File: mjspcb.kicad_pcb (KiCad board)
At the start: 2 copper layers, 97.2 x 55.9 mm, 83 parts, among them P1 Batteries, P10 Lipo, P11 grove i2c, P12 grove analog, P13 grove analog, P14 HPMA115S0-XXX, P15 piggyback, P2 serial breakout, P3 I2C breakout, P4 GPS, P5 piezo, P6 BPW34, P7 electrodes, P8 perfboard breakout, P9 reset, Q1 STU60N3LH5, Q2 STU60N3LH5, U1 ATMEGA328P, U2 RFM95W, U3 MCP1700-3302

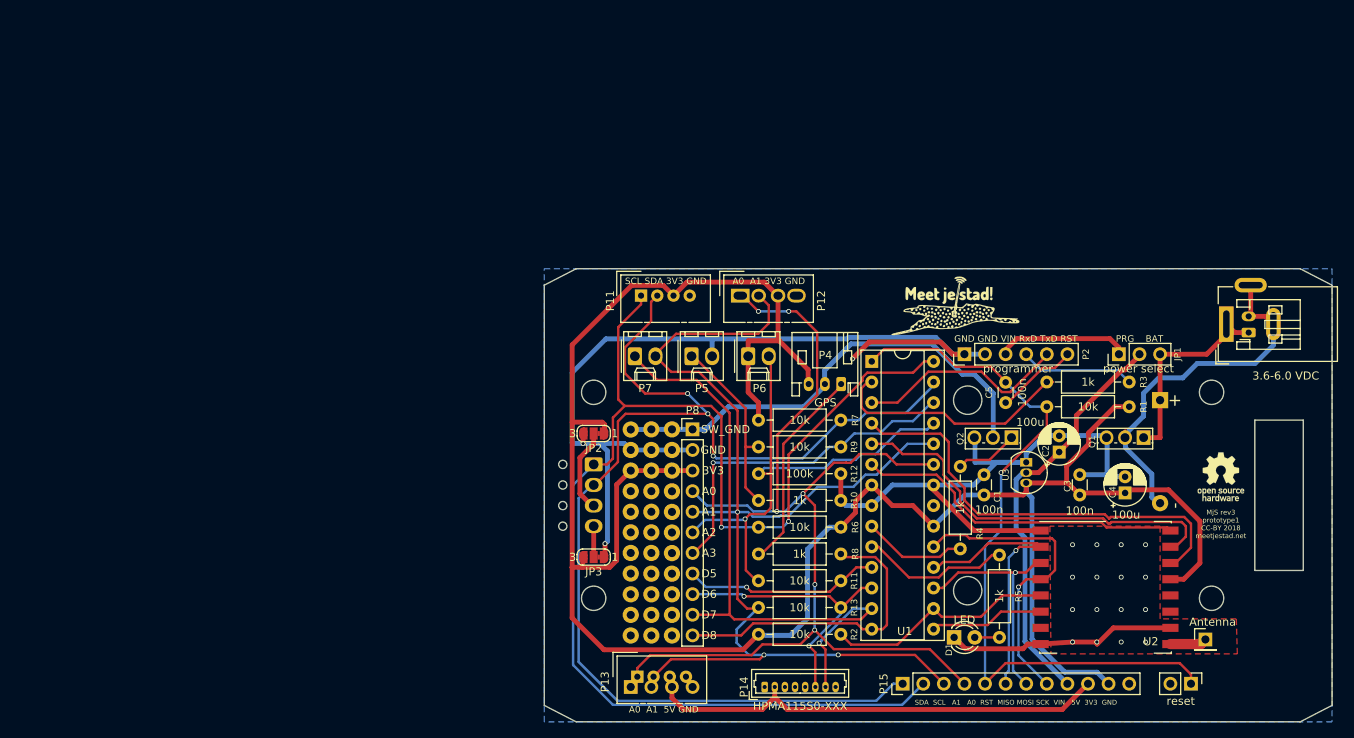
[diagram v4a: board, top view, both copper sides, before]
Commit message: Replace with MJS2020-PROTO2 redesign
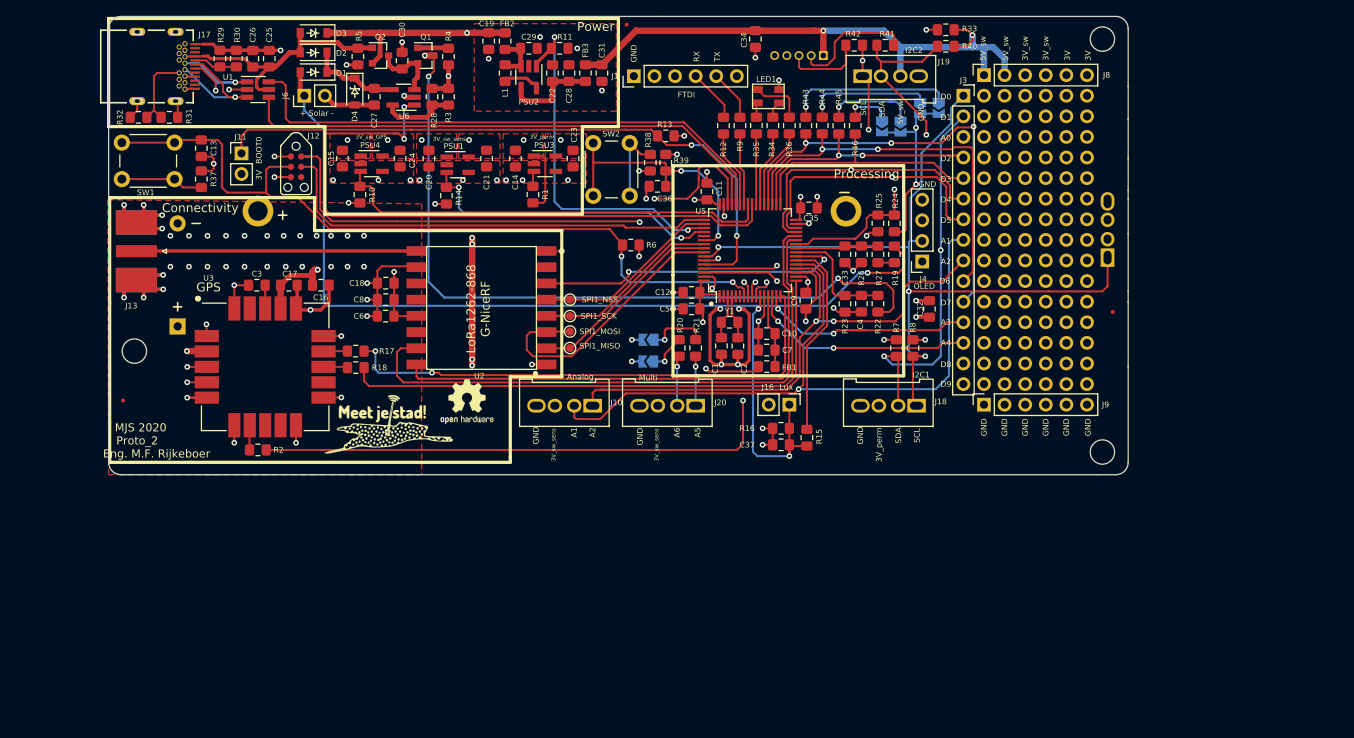
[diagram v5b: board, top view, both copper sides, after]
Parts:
- removed ? (x33): , meetjestad:perf
- removed AE1: Antenna, Connector_PinHeader_2.54mm:PinHeader_1x01_P2.54mm_Vertical
- removed DC1: 2.7 - 6.0 VDC, Connector_BarrelJack:BarrelJack_Wuerth_6941xx301002
- removed H4: MountingHole, MountingHole:MountingHole_3mm
- removed JP1: power select, Connector_PinHeader_2.54mm:PinHeader_1x03_P2.54mm_Vertical
- removed JP2: V1, meetjestad:SolderJumper-3_P1.3mm_Bridged12_RoundedPad1.0x1.5mm_NumberLabels
- removed JP3: V2, meetjestad:SolderJumper-3_P1.3mm_Bridged12_RoundedPad1.0x1.5mm_NumberLabels
- removed LOGO1: Open source hardware, Symbol:OSHW-Logo_5.7x6mm_SilkScreen
- removed LOGO2: MJS Logo, meetjestad:mjs
- removed P1: Batteries, Battery:BatteryHolder_Keystone_2479_3xAAA
- removed P10: Lipo, Connector_JST:JST_PH_S2B-PH-K_1x02_P2.00mm_Horizontal
- removed P11: grove i2c, Connector:NS-Tech_Grove_1x04_P2mm_Vertical
- removed P12: grove analog, meetjestad:NS-Tech_Grove_1x04_P2mm_P2.54mm_Vertical
- removed P13: grove analog, meetjestad:NS-Tech_Grove_1x04_P2mm_P2.54mm_Vertical_Alternative
- removed P14: HPMA115S0-XXX, Connector_Molex:Molex_PicoBlade_53047-0810_1x08_P1.25mm_Vertical
- removed P15: piggyback, Connector_PinHeader_2.54mm:PinHeader_1x12_P2.54mm_Vertical
- removed P2: serial breakout, Connector_PinHeader_2.54mm:PinHeader_1x06_P2.54mm_Vertical
- removed P3: I2C breakout, meetjestad:Molex_KK-254_44812-0004_1x04_P2.54mm_Vertical
- removed P4: GPS, Connector_JST:JST_PH_S3B-PH-K_1x03_P2.00mm_Horizontal
- removed P5: piezo, Connector_Molex:Molex_KK-254_AE-6410-02A_1x02_P2.54mm_Vertical
- removed P6: BPW34, Connector_Molex:Molex_KK-254_AE-6410-02A_1x02_P2.54mm_Vertical
- removed P7: electrodes, Connector_Molex:Molex_KK-254_AE-6410-02A_1x02_P2.54mm_Vertical
- removed P8: perfboard breakout, Connector_PinHeader_2.54mm:PinHeader_1x11_P2.54mm_Vertical
- removed P9: reset, Connector_PinHeader_2.54mm:PinHeader_1x02_P2.54mm_Vertical
- added C10: 100nF, Capacitor_SMD:C_0805_2012Metric_Pad1.15x1.40mm_HandSolder, F.Cu at (161.0, 100.7)
- added C11: 100nF, Capacitor_SMD:C_0805_2012Metric_Pad1.15x1.40mm_HandSolder, F.Cu at (153.7, 83.2)
- added C12: 100nF, Capacitor_SMD:C_0805_2012Metric_Pad1.15x1.40mm_HandSolder, F.Cu at (151.8, 95.6)
- added C13: 100nF, Capacitor_SMD:C_0805_2012Metric_Pad1.15x1.40mm_HandSolder, F.Cu at (91.3, 77.9)
- added C14: 1uF, Capacitor_SMD:C_0805_2012Metric_Pad1.15x1.40mm_HandSolder, F.Cu at (130.0, 79.1)
- added C15: 1uF, Capacitor_SMD:C_0805_2012Metric_Pad1.15x1.40mm_HandSolder, F.Cu at (108.7, 79.1)
- added C16: 4.7uF, Capacitor_SMD:C_0805_2012Metric_Pad1.15x1.40mm_HandSolder, F.Cu at (106.0, 94.7)
- added C17: 100nF, Capacitor_SMD:C_0805_2012Metric_Pad1.15x1.40mm_HandSolder, F.Cu at (102.1, 94.7)
- added C18: 4.7uF, Capacitor_SMD:C_0805_2012Metric_Pad1.15x1.40mm_HandSolder, F.Cu at (114.1, 94.5)
- added C19: 1uF, Capacitor_SMD:C_0805_2012Metric_Pad1.15x1.40mm_HandSolder, F.Cu at (126.7, 64.6)
- added C20: 1uF, Capacitor_SMD:C_0805_2012Metric_Pad1.15x1.40mm_HandSolder, F.Cu at (119.4, 79.1)
- added C21: 1uF, Capacitor_SMD:C_0805_2012Metric_Pad1.15x1.40mm_HandSolder, F.Cu at (126.5, 79.1)
- added C22: 4.7uF, Capacitor_SMD:C_0805_2012Metric_Pad1.15x1.40mm_HandSolder, F.Cu at (134.6, 68.6)
- added C23: 1uF, Capacitor_SMD:C_0805_2012Metric_Pad1.15x1.40mm_HandSolder, F.Cu at (137.2, 79.1)
- added C24: 1uF, Capacitor_SMD:C_0805_2012Metric_Pad1.15x1.40mm_HandSolder, F.Cu at (115.8, 79.1)
- added C25: 100nF, Capacitor_SMD:C_0805_2012Metric_Pad1.15x1.40mm_HandSolder, F.Cu at (99.7, 66.8)
- added C26: 1uF, Capacitor_SMD:C_0805_2012Metric_Pad1.15x1.40mm_HandSolder, F.Cu at (97.7, 66.8)
- added C27: 4.7uF, Capacitor_SMD:C_0805_2012Metric_Pad1.15x1.40mm_HandSolder, F.Cu at (112.6, 71.5)
- added C28: 4.7uF, Capacitor_SMD:C_0805_2012Metric_Pad1.15x1.40mm_HandSolder, F.Cu at (136.7, 68.6)
- added C29: 4.7uF, Capacitor_SMD:C_0805_2012Metric_Pad1.15x1.40mm_HandSolder, F.Cu at (131.7, 65.5)
- added C30: 4.7uF, Capacitor_SMD:C_0805_2012Metric_Pad1.15x1.40mm_HandSolder, F.Cu at (116.1, 67.0)
- added C31: 1uF, Capacitor_SMD:C_0805_2012Metric_Pad1.15x1.40mm_HandSolder, F.Cu at (140.7, 68.6)
- added C32: 100nF, Capacitor_SMD:C_0805_2012Metric_Pad1.15x1.40mm_HandSolder, F.Cu at (181.1, 97.7)
- added C33: 100nF, Capacitor_SMD:C_0805_2012Metric_Pad1.15x1.40mm_HandSolder, F.Cu at (170.7, 90.9)
- added C34: 100nF, Capacitor_SMD:C_0805_2012Metric_Pad1.15x1.40mm_HandSolder, F.Cu at (159.6, 64.4)
- added C35: 100nF, Capacitor_SMD:C_0805_2012Metric_Pad1.15x1.40mm_HandSolder, F.Cu at (166.2, 85.2)
- added C36: 100nF, Capacitor_SMD:C_0805_2012Metric_Pad1.15x1.40mm_HandSolder, F.Cu at (147.6, 82.5)
- added C37: 100nF, Capacitor_SMD:C_0805_2012Metric_Pad1.15x1.40mm_HandSolder, F.Cu at (162.8, 114.4)
- added C6: 100nF, Capacitor_SMD:C_0805_2012Metric_Pad1.15x1.40mm_HandSolder, F.Cu at (114.0, 98.6)
- added C7: 1uF, Capacitor_SMD:C_0805_2012Metric_Pad1.15x1.40mm_HandSolder, F.Cu at (161.0, 102.7)
- added C8: 4.7uF, Capacitor_SMD:C_0805_2012Metric_Pad1.15x1.40mm_HandSolder, F.Cu at (114.1, 96.5)
- added C9: 100nF, Capacitor_SMD:C_0805_2012Metric_Pad1.15x1.40mm_HandSolder, F.Cu at (165.9, 96.6)
- added D2: MBR120VLSFT3G, meetjestad:Diode_SMD-SOD_123, F.Cu at (105.4, 63.3)
- added D3: MBR120VLSFT3G, meetjestad:Diode_SMD-SOD_123, F.Cu at (105.4, 60.9)
- added D4: 6,2V, meetjestad:D_SOD-123, F.Cu at (112.9, 71.0)
- added FB1: Ferrite_Bead, Resistor_SMD:R_0805_2012Metric_Pad1.15x1.40mm_HandSolder, F.Cu at (161.0, 104.8)
- added FB2: Ferrite_Bead, Resistor_SMD:R_0805_2012Metric_Pad1.15x1.40mm_HandSolder, F.Cu at (128.8, 64.6)
- added FB3: Ferrite_Bead, Resistor_SMD:R_0805_2012Metric_Pad1.15x1.40mm_HandSolder, F.Cu at (138.7, 68.6)
- added FID1: Fiducial, Fiducial:Fiducial_0.5mm_Mask1mm, F.Cu at (81.7, 109.0)
- added FID2: Fiducial, Fiducial:Fiducial_0.5mm_Mask1mm, F.Cu at (143.8, 62.6)
- added FID3: Fiducial, Fiducial:Fiducial_0.5mm_Mask1mm, F.Cu at (203.7, 98.0)
- added J1: FTDI, Connector_PinHeader_2.54mm:PinHeader_1x06_P2.54mm_Vertical, F.Cu at (144.7, 69.0)
- added J10: Analog, meetjestad:Grove_4pin&Header_4pin, F.Cu at (135.7, 108.3)
- added J11: BOOT0, Connector_PinHeader_2.54mm:PinHeader_1x02_P2.54mm_Vertical, F.Cu at (96.3, 78.5)
- added J12: Tag connect, meetjestad:Tag connect, F.Cu at (102.4, 78.9)
- added J13: Conn_Coaxial, meetjestad:SMA connector edge mount, F.Cu at (79.0, 97.8)
- added J14: Lithium Ion, meetjestad:BatteryHolder_18650-PC2, B.Cu at (134.6, 85.6)
- added J15: Temp/Hum, meetjestad:Grove_4pin&Header_4pin, B.Cu at (201.8, 87.5)
- added J16: BPW34, Connector_PinHeader_2.54mm:PinHeader_1x02_P2.54mm_Vertical, F.Cu at (163.8, 109.5)
- added J17: USB_C_connector, 632723300011_Eagle_WR-USB_rev20b:632723100011, F.Cu at (84.6, 67.8)
- added J18: I2C 3V_perm, meetjestad:Grove_4pin&Header_4pin, F.Cu at (175.7, 108.3)
- added J19: I2C 5V_SW, meetjestad:Grove_4pin&Header_4pin, F.Cu at (176.7, 70.2)
- added J20: Multi, meetjestad:Grove_4pin&Header_4pin, F.Cu at (148.4, 108.3)
- added J3: Prototype header, Connector_PinSocket_2.54mm:PinSocket_1x15_P2.54mm_Vertical, F.Cu at (185.3, 71.4)
- added J4: Oled, Connector_PinSocket_2.54mm:PinSocket_1x04_P2.54mm_Vertical, F.Cu at (180.2, 91.8)
- added J5: Conn_01x02_Male, meetjestad:Battery__holder, B.Cu at (110.0, 110.0)
- added J6: Solar, Connector_PinHeader_2.54mm:PinHeader_1x02_P2.54mm_Vertical, F.Cu at (104.0, 71.4)
- added J7: Particulate matter, meetjestad:B5B-ZR, B.Cu at (165.5, 63.9)
- added J8: Prototype power, Connector_PinSocket_2.54mm:PinSocket_1x06_P2.54mm_Vertical, F.Cu at (187.8, 68.8)
- added J9: Prototype GND, Connector_PinSocket_2.54mm:PinSocket_1x06_P2.54mm_Vertical, F.Cu at (187.8, 109.5)
- added L1: 4.7uH, Resistor_SMD:R_0805_2012Metric_Pad1.15x1.40mm_HandSolder, F.Cu at (128.8, 68.6)
- added LED1: JT-S3030_RGB_LED, meetjestad:JT-S3030_RGB_LED, F.Cu at (160.0, 70.6)
- added Logo_kitt1: Logo_Open_Hardware_Small, meetjestad:Kitt_logo, B.Cu at (86.4, 109.6)
- added Logo_mjs1: Logo_Open_Hardware_Small, meetjestad:mjs_logo, F.Cu at (113.7, 107.4)
- added Logo_mjs2: Logo_Open_Hardware_Small, Symbol:OSHW-Logo2_7.3x6mm_SilkScreen, F.Cu at (124.1, 109.1)
- added PSU1: TPS7A02, Package_TO_SOT_SMD:SOT-23-5_HandSoldering, F.Cu at (122.9, 79.9)
- added PSU2: XC9140A501MR-G, Package_TO_SOT_SMD:SOT-23-5_HandSoldering, F.Cu at (131.7, 69.1)
- added PSU3: TPS7A02, Package_TO_SOT_SMD:SOT-23-5_HandSoldering, F.Cu at (133.7, 79.8)
- added PSU4: TPS7A02, Package_TO_SOT_SMD:SOT-23-5_HandSoldering, F.Cu at (112.3, 79.8)
- added R14: 100k, Resistor_SMD:R_0805_2012Metric_Pad1.15x1.40mm_HandSolder, F.Cu at (121.5, 83.7)
- added R15: 10k, Resistor_SMD:R_0805_2012Metric_Pad1.15x1.40mm_HandSolder, F.Cu at (166.0, 113.5)
- added R16: 100k, Resistor_SMD:R_0805_2012Metric_Pad1.15x1.40mm_HandSolder, F.Cu at (162.8, 112.4)
- added R17: 1k, Resistor_SMD:R_0805_2012Metric_Pad1.15x1.40mm_HandSolder, F.Cu at (110.4, 102.9)
- added R18: 1k, Resistor_SMD:R_0805_2012Metric_Pad1.15x1.40mm_HandSolder, F.Cu at (110.4, 104.9)
- added R19: 1M, Resistor_SMD:R_0805_2012Metric_Pad1.15x1.40mm_HandSolder, F.Cu at (176.8, 90.9)
- added R20: 10k, Resistor_SMD:R_0805_2012Metric_Pad1.15x1.40mm_HandSolder, F.Cu at (150.2, 102.5)
- added R21: 10k, Resistor_SMD:R_0805_2012Metric_Pad1.15x1.40mm_HandSolder, F.Cu at (152.3, 102.5)
- added R22: 1M, Resistor_SMD:R_0805_2012Metric_Pad1.15x1.40mm_HandSolder, F.Cu at (174.8, 97.0)
- added R23: 1M, Resistor_SMD:R_0805_2012Metric_Pad1.15x1.40mm_HandSolder, F.Cu at (170.7, 97.0)
- added R24: 1M, Resistor_SMD:R_0805_2012Metric_Pad1.15x1.40mm_HandSolder, F.Cu at (176.8, 87.1)
- added R25: 100k, Resistor_SMD:R_0805_2012Metric_Pad1.15x1.40mm_HandSolder, F.Cu at (174.8, 87.1)
- added R26: 1M, Resistor_SMD:R_0805_2012Metric_Pad1.15x1.40mm_HandSolder, F.Cu at (174.8, 90.9)
- added R27: 1M, Resistor_SMD:R_0805_2012Metric_Pad1.15x1.40mm_HandSolder, F.Cu at (172.7, 90.9)
- added R28: 10k, Resistor_SMD:R_0805_2012Metric_Pad1.15x1.40mm_HandSolder, F.Cu at (119.8, 71.5)
- added R29: 10k, Resistor_SMD:R_0805_2012Metric_Pad1.15x1.40mm_HandSolder, F.Cu at (93.6, 66.8)
- added R30: 10k, Resistor_SMD:R_0805_2012Metric_Pad1.15x1.40mm_HandSolder, F.Cu at (95.6, 66.8)
- added R31: 10k, Resistor_SMD:R_0805_2012Metric_Pad1.15x1.40mm_HandSolder, F.Cu at (87.4, 74.0)
- added R32: 10k, Resistor_SMD:R_0805_2012Metric_Pad1.15x1.40mm_HandSolder, F.Cu at (83.6, 74.0)
- added R33: 10k, Resistor_SMD:R_0805_2012Metric_Pad1.15x1.40mm_HandSolder, F.Cu at (183.1, 63.2)
- added R34: 1k, Resistor_SMD:R_0805_2012Metric_Pad1.15x1.40mm_HandSolder, F.Cu at (161.8, 75.0)
- added R35: 1k, Resistor_SMD:R_0805_2012Metric_Pad1.15x1.40mm_HandSolder, F.Cu at (159.8, 75.0)
- added R36: 1k, Resistor_SMD:R_0805_2012Metric_Pad1.15x1.40mm_HandSolder, F.Cu at (163.8, 75.0)
- added R37: 100, Resistor_SMD:R_0805_2012Metric_Pad1.15x1.40mm_HandSolder, F.Cu at (91.3, 81.7)
- added R38: 100, Resistor_SMD:R_0805_2012Metric_Pad1.15x1.40mm_HandSolder, F.Cu at (146.7, 79.6)
- added R39: 10k, Resistor_SMD:R_0805_2012Metric_Pad1.15x1.40mm_HandSolder, F.Cu at (148.6, 79.6)
- added R40: 10k, Resistor_SMD:R_0805_2012Metric_Pad1.15x1.40mm_HandSolder, F.Cu at (183.1, 65.3)
- added R41: 1k, Resistor_SMD:R_0805_2012Metric_Pad1.15x1.40mm_HandSolder, F.Cu at (175.7, 65.2)
- added R42: 1k, Resistor_SMD:R_0805_2012Metric_Pad1.15x1.40mm_HandSolder, F.Cu at (171.8, 65.2)
- added R43: 10k, Resistor_SMD:R_0805_2012Metric_Pad1.15x1.40mm_HandSolder, F.Cu at (165.9, 75.0)
- added R44: 10k, Resistor_SMD:R_0805_2012Metric_Pad1.15x1.40mm_HandSolder, F.Cu at (167.9, 75.0)
- added R45: 10k, Resistor_SMD:R_0805_2012Metric_Pad1.15x1.40mm_HandSolder, F.Cu at (169.9, 75.1)
- added R46: 10k, Resistor_SMD:R_0805_2012Metric_Pad1.15x1.40mm_HandSolder, F.Cu at (172.0, 75.1)
- added SP1: SolderJumper_2_Open, Jumper:SolderJumper-2_P1.3mm_Open_TrianglePad1.0x1.5mm, B.Cu at (146.4, 104.1)
- added SP2: SolderJumper_2_Open, Jumper:SolderJumper-2_P1.3mm_Open_TrianglePad1.0x1.5mm, B.Cu at (146.5, 101.5)
- added SP3: SolderJumper_2_Open, Jumper:SolderJumper-2_P1.3mm_Open_TrianglePad1.0x1.5mm, B.Cu at (182.2, 72.9)
- added SP4: SolderJumper_2_Open, Jumper:SolderJumper-2_P1.3mm_Open_TrianglePad1.0x1.5mm, B.Cu at (180.0, 72.9)
- added SP5: SolderJumper_2_Open, Jumper:SolderJumper-2_P1.3mm_Open_TrianglePad1.0x1.5mm, B.Cu at (177.5, 75.2)
- added SP6: SolderJumper_2_Open, Jumper:SolderJumper-2_P1.3mm_Open_TrianglePad1.0x1.5mm, B.Cu at (175.3, 75.1)
- added SW1: SW_Push, Button_Switch_THT:SW_PUSH_6mm, F.Cu at (88.0, 81.7)
- added SW2: SW_Push, Button_Switch_THT:SW_PUSH_6mm, F.Cu at (144.1, 77.2)
- added TP1: TestPoint_Small, TestPoint:TestPoint_Pad_D1.0mm, F.Cu at (136.8, 96.5)
- added TP2: TestPoint_Small, TestPoint:TestPoint_Pad_D1.0mm, F.Cu at (136.8, 98.6)
- added TP3: TestPoint_Small, TestPoint:TestPoint_Pad_D1.0mm, F.Cu at (136.8, 100.5)
- added TP4: TestPoint_Small, TestPoint:TestPoint_Pad_D1.0mm, F.Cu at (136.8, 102.5)
- added TP5: Sticker field, meetjestad:Sticker field, B.Cu at (110.0, 117.3)
- added TP6: Flash OK, meetjestad:Flash OK, B.Cu at (132.8, 113.7)
- added TP7: Test OK, meetjestad:Test OK, B.Cu at (159.3, 115.7)
- added U4: PrototypeGrid, meetjestad:Prototype grid, F.Cu at (187.8, 71.4)
- added U5: STM32L072RBTx-meetjestad, meetjestad:STM32F072_LQFP-64, F.Cu at (151.0, 90.4)
- added U6: MCP73831, Package_TO_SOT_SMD:SOT-23-5_HandSoldering, F.Cu at (116.3, 71.6)
- added Y1: 32kHz, Resistor_SMD:R_0805_2012Metric_Pad1.15x1.40mm_HandSolder, F.Cu at (156.5, 99.3)
- C1: value 100n -> 12.5pF; footprint Capacitor_THT:C_Disc_D3.0mm_W1.6mm_P2.50mm -> Capacitor_SMD:C_0805_2012Metric_Pad1.15x1.40mm_HandSolder
- C2: value 100u -> 12.5pF; footprint Capacitor_THT:CP_Radial_D5.0mm_P2.00mm -> Capacitor_SMD:C_0805_2012Metric_Pad1.15x1.40mm_HandSolder
- C3, C5: value 100n -> 100nF; footprint Capacitor_THT:C_Disc_D3.0mm_W1.6mm_P2.50mm -> Capacitor_SMD:C_0805_2012Metric_Pad1.15x1.40mm_HandSolder
- C4: value 100u -> 100nF; footprint Capacitor_THT:CP_Radial_D5.0mm_P2.00mm -> Capacitor_SMD:C_0805_2012Metric_Pad1.15x1.40mm_HandSolder
- D1: value LED -> MBR120VLSFT3G; footprint LED_THT:LED_D3.0mm -> meetjestad:Diode_SMD-SOD_123
- H1, H2, H3: footprint MountingHole:MountingHole_3mm -> meetjestad:Mounting_hole
- Q1, Q2: value STU60N3LH5 -> DMP2035U-7; footprint Package_TO_SOT_THT:TO-251-3_Vertical -> Package_TO_SOT_SMD:SOT-23
- R1, R2, R9: value 10k -> 1k; footprint Resistor_THT:R_Axial_DIN0207_L6.3mm_D2.5mm_P10.16mm_Horizontal -> Resistor_SMD:R_0805_2012Metric_Pad1.15x1.40mm_HandSolder
- R10: value 1k -> 100k; footprint Resistor_THT:R_Axial_DIN0207_L6.3mm_D2.5mm_P10.16mm_Horizontal -> Resistor_SMD:R_0805_2012Metric_Pad1.15x1.40mm_HandSolder
- R11: value 10k -> 100k; footprint Resistor_THT:R_Axial_DIN0207_L6.3mm_D2.5mm_P10.16mm_Horizontal -> Resistor_SMD:R_0805_2012Metric_Pad1.15x1.40mm_HandSolder
- R12: value 100k -> 1k; footprint Resistor_THT:R_Axial_DIN0207_L6.3mm_D2.5mm_P10.16mm_Horizontal -> Resistor_SMD:R_0805_2012Metric_Pad1.15x1.40mm_HandSolder
- R13, R6, R7: footprint Resistor_THT:R_Axial_DIN0207_L6.3mm_D2.5mm_P10.16mm_Horizontal -> Resistor_SMD:R_0805_2012Metric_Pad1.15x1.40mm_HandSolder
- R3, R4, R5, R8: value 1k -> 10k; footprint Resistor_THT:R_Axial_DIN0207_L6.3mm_D2.5mm_P10.16mm_Horizontal -> Resistor_SMD:R_0805_2012Metric_Pad1.15x1.40mm_HandSolder
- U1: value ATMEGA328P -> USBLC-2SC6; footprint Package_DIP:DIP-28_W7.62mm_Socket -> Package_TO_SOT_SMD:SOT-23-6_Handsoldering
- U2: value RFM95W -> LoRa_1262_G-NiceRF; footprint RF_Module:HOPERF_RFM9XW_SMD -> meetjestad:LoRa_1262_G-NiceRF
- U3: value MCP1700-3302 -> GPS; footprint Package_TO_SOT_THT:TO-92_Inline -> meetjestad:GPS_ublox-SAM-M8Q
- moved D1 107.0 mm to (105.4, 65.7)
- moved C3 104.7 mm to (98.2, 94.7), turned to 0 degrees
- moved Q1 100.3 mm to (119.0, 66.4), turned to 0 degrees
- moved R5 100.2 mm to (110.6, 66.5)
- moved U3 96.2 mm to (99.4, 94.6), turned to 0 degrees
- moved R3 91.0 mm to (121.8, 71.5), turned to 90 degrees
- moved Q2 91.0 mm to (113.4, 66.4), turned to 0 degrees
- moved U1 82.8 mm to (98.3, 70.6)
- moved R4 80.9 mm to (121.8, 66.5)
- moved R1 78.0 mm to (132.2, 83.6), turned to 270 degrees
- moved H1 76.4 mm to (202.4, 64.4)
- moved U2 74.2 mm to (133.9, 104.5), turned to 180 degrees
- moved R11 70.1 mm to (135.5, 65.5)
- moved R2 65.8 mm to (98.3, 115.1), turned to 180 degrees
- moved H2 64.3 mm to (83.1, 102.9)
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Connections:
- C1 pad 1: VCC -> Net-(C1-Pad1)
- C2 pad 1: VIN -> Net-(C2-Pad1)
- C3 pad 1: VCC -> GND
- C3 pad 2: GND -> Net-(C3-Pad2)
- C4 pad 1: VCC -> PC4
- C5 pad 1: Net-(C5-Pad1) -> 3V-perm_CPU
- C5 pad 2: RST -> GND
- D1 pad 1: GND -> Solar
- D1 pad 2: Net-(D1-Pad2) -> Net-(C27-Pad2)
- Q1 pad 1: +BATT -> Net-(Q1-Pad1)
- Q1 pad 2: -BATT -> Net-(C30-Pad1)
- Q1 pad 3: GND -> +BATT
- Q2 pad 1: Net-(Q2-Pad1) -> VBUS
- Q2 pad 2: SW_GND -> Vin
- Q2 pad 3: GND -> Net-(C30-Pad1)
- R1 pad 1: VCC -> Net-(PSU3-Pad3)
- R1 pad 2: RST -> Vin
- R10 pad 1: Net-(P5-Pad1) -> PA8
- R11 pad 1: A2 -> PC10
- R11 pad 2: D5 -> GND
- R12 pad 1: A2 -> Net-(J1-Pad4)
- R12 pad 2: GND -> PA10
- R13 pad 1: A1 -> BOOT0
- R13 pad 2: D6 -> GND
- R2 pad 1: VCC -> PC2
- R2 pad 2: D10 -> Net-(R2-Pad2)
- R3 pad 2: RXD -> GND
- R4 pad 1: Net-(Q2-Pad1) -> Net-(Q1-Pad1)
- R4 pad 2: X1 -> GND
- R5 pad 1: X2 -> VBUS
- R5 pad 2: Net-(D1-Pad2) -> GND
- R6 pad 1: VCC -> 3V-perm_CPU
- R6 pad 2: SCL -> NRST
- R7 pad 1: VCC -> PB7
- R7 pad 2: SDA -> 3V-perm_CPU
- R8 pad 1: Net-(P4-Pad1) -> PB6
- R8 pad 2: D8 -> 3V-perm_CPU
- R9 pad 1: Net-(P5-Pad1) -> Net-(J1-Pad5)
- R9 pad 2: A3 -> PA9
- U1 pad 1: RST -> Net-(J17-PadA7)
- U1 pad 2: RXD -> GND
- U1 pad 3: TXD -> Net-(J17-PadA6)
- U1 pad 4: D2 -> PA12
- U1 pad 5: D3 -> VBUS
- U1 pad 6: D4 -> PA11
- U2 pad 13: VCC -> 3V-perm_CPU
- U2 pad 14: D2 -> Net-(U2-Pad14)
- U2 pad 15: D3 -> PB1
- U2 pad 16: D4 -> PB2
- U2 pad 2: MISO -> PB4
- U2 pad 3: MOSI -> PB5
- U2 pad 4: SCK -> PB3
- U2 pad 5: D10 -> PA15
- U2 pad 6: D9 -> PA7
- U3 pad 2: VIN -> 3V-sw_GPS
- U3 pad 3: VCC -> 3V-perm_CPU
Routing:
- net VCC: track 280.6 -> 0.00 mm
- net 3V-sw_sens: track 0.00 -> 199.2 mm, vias 0 -> 9
- net SCL: track 164.4 -> 0.00 mm, vias 2 -> 0
- net SDA: track 146.8 -> 0.00 mm, vias 3 -> 0
- net +BATT: track 26.0 -> 168.7 mm, vias 0 -> 3
- net A1: track 141.9 -> 0.00 mm, vias 3 -> 0
- net A0: track 134.9 -> 0.00 mm, vias 6 -> 0
- net Solar: track 0.00 -> 106.8 mm, vias 0 -> 1
- net PB6: track 0.00 -> 100.0 mm, vias 0 -> 3
- net PB7: track 0.00 -> 98.4 mm, vias 0 -> 3
- net NRST: track 0.00 -> 97.5 mm, vias 0 -> 2
- net RST: track 91.2 -> 0.00 mm, vias 1 -> 0
- net 3V-perm_CPU: track 0.00 -> 88.3 mm, vias 0 -> 15
- net PA5: track 0.00 -> 87.6 mm, vias 0 -> 1
- net PC2: track 0.00 -> 83.8 mm, vias 0 -> 2
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- added copper zone on F.Cu, net 3V-perm_CPU
- added copper zone on In2.Cu, net 3V-perm_CPU
- added copper zone on F.Cu, net 3V-sw_GPS
- added copper zone on F.Cu, net 3V-sw_sens
- added copper zone on In1.Cu, net GND
- added copper zone on F.Cu, net Vin
- removed copper zone on B.Cu, net GND
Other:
- board size 97.2 x 55.9 mm -> 125.7 x 56.5 mm
- copper layers 2 -> 4
- net class 3v cpu added: clearance 0.2, trace_width 0.35, via_dia 0.7, via_drill 0.35
- net class Antenna added: clearance 0.9, trace_width 0.43, via_dia 0.7, via_drill 0.35
- net class Default: trace_width 0.3 -> 0.25; via_dia 0.6 -> 0.7; via_drill 0.4 -> 0.35
- net class antenna removed
- net class power: clearance 0.2 -> 0.3; via_dia 0.6 -> 0.7; via_drill 0.4 -> 0.35
- rule pad_to_mask_clearance: 0 -> 0.051
- board text added: "+ Solar -"
- board text added: "3V"
- board text added: "3V_perm"
- board text added: "3V_sw"
- board text added: "3V_sw_GPS"
- board text added: "3V_sw_sens"
- board text added: "5V_sw"
- board text added: "A4"
- board text added: "A5"
- board text added: "A6"
- board text added: "Analog"
- board text added: "BOOT0"
- board text added: "Connectivity"
- board text added: "D0"
- board text added: "D1"
- board text added: "D2"
- board text added: "D3"
- board text added: "D4"
- board text added: "D9"
- board text added: "FTDI"
- board text added: "GPS"
- board text added: "I2C1"
- board text added: "I2C2"
- board text added: "I2C2_SCL"
- board text added: "I2C2_SDA"
- board text added: "LoRa1262-868 G-NiceRF"
- board text added: "Lux"
- board text added: "MJS 2020 Proto_2 Eng. M.F. Rijkeboer"
- board text added: "Multi"
- board text added: "OLED"
- board text added: "Particulate matter"
- board text added: "Power"
- board text added: "Processing"
- board text added: "RX"
- board text added: "SCL"
- board text added: "SDA"
- board text added: "SPI1_MISO"
- board text added: "SPI1_MOSI"
- board text added: "SPI1_NSS"
- board text added: "SPI1_SCK"
- board text added: "TX"
- board text added: "Temp/hum"
- board text removed: "+"
- board text removed: "-"
- board text removed: "3.6-6.0 VDC"
- board text removed: "3V3"
- board text removed: "A0 A1 3V3 GND"
- board text removed: "A0 A1 5V GND"
- board text removed: "GND GND VIN RxD TxD RST"
- board text removed: "I2C breakout"
- board text removed: "ID"
- board text removed: "MjS rev3 prototype1 CC-BY 2018 meetjestad.net"
- board text removed: "PRG BAT"
- board text removed: "SCL SDA 3V3 GND"
- board text removed: "SDA SCL A1 A0 RST MISO MOSI SCK VIN 5V 3V3 GND"
- board text removed: "SW_GND"
- board text removed: "power select"
- board text removed: "programmer"

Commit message: Update to MJS2020-PROTO3
See CHANGELOG.md for detailed changes.
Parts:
- removed J11: BOOT0, Connector_PinHeader_2.54mm:PinHeader_1x02_P2.54mm_Vertical
- removed LED1: JT-S3030_RGB_LED, meetjestad:JT-S3030_RGB_LED
- removed the PSU1 at (122.9, 79.9)
- removed SP3, SP4, SP5, SP6: SolderJumper_2_Open, Jumper:SolderJumper-2_P1.3mm_Open_TrianglePad1.0x1.5mm
- removed TP1, TP2, TP3, TP4: TestPoint_Small, TestPoint:TestPoint_Pad_D1.0mm
- added C38: 100nF, Capacitor_SMD:C_0805_2012Metric_Pad1.15x1.40mm_HandSolder, F.Cu at (167.9, 78.9)
- added C39: 100nF, Capacitor_SMD:C_0805_2012Metric_Pad1.15x1.40mm_HandSolder, B.Cu at (216.8, 85.1)
- added C40: 100nF, Capacitor_SMD:C_0805_2012Metric_Pad1.15x1.40mm_HandSolder, B.Cu at (182.9, 91.4)
- added D5: LED, LED_SMD:LED_0805_2012Metric, F.Cu at (114.6, 74.9)
- added D6: LED_RGB, meetjestad:JTS3535, F.Cu at (140.6, 86.0)
- added J2: Conn_01x16_Female, Connector_PinSocket_2.54mm:PinSocket_1x16_P2.54mm_Vertical, F.Cu at (185.4, 109.2)
- added Logo_mjs3: Logo_Open_Hardware_Small, meetjestad:mjs-logo-22mm, F.Cu at (106.7, 106.4)
- added Logo_mjs4: Logo_Open_Hardware_Small, Symbol:OSHW-Logo2_7.3x6mm_SilkScreen, B.Cu at (180.8, 75.9)
- added PSU2: TPS7A02, Package_TO_SOT_SMD:SOT-23-5_HandSoldering, F.Cu at (122.9, 82.2)
- added R47: 1M, Resistor_SMD:R_0805_2012Metric_Pad1.15x1.40mm_HandSolder, F.Cu at (165.9, 78.9)
- added R48: 10k, Resistor_SMD:R_0805_2012Metric_Pad1.15x1.40mm_HandSolder, F.Cu at (122.2, 74.9)
- added R49: 10k, Resistor_SMD:R_0805_2012Metric_Pad1.15x1.40mm_HandSolder, B.Cu at (172.3, 81.8)
- added R50: 10k, Resistor_SMD:R_0805_2012Metric_Pad1.15x1.40mm_HandSolder, B.Cu at (176.2, 80.8)
- added SW3: SW_Push, meetjestad:Switch_Header2.54_Combi, F.Cu at (96.5, 76.2)
- added U7: MCP9808_MSOP, Package_SO:MSOP-8_3x3mm_P0.65mm, B.Cu at (216.5, 90.2)
- added U8: SST26VF032B, Package_SO:SOIJ-8_5.3x5.3mm_P1.27mm, B.Cu at (179.4, 85.3)
- H1, H2, H3: footprint meetjestad:Mounting_hole -> MountingHole:MountingHole_3.2mm_M3
- J10, J18, J19, J20: footprint meetjestad:Grove_4pin&Header_4pin -> meetjestad:2,54_2.0pitchCombi
- J12: value Tag connect -> SWD; footprint meetjestad:Tag connect -> Connector_PinHeader_2.54mm:PinHeader_1x06_P2.54mm_Vertical
- J14: footprint meetjestad:BatteryHolder_18650-PC2 -> meetjestad:Combi_2.0_2.45pitch_2PIN
- J15: footprint meetjestad:Grove_4pin&Header_4pin -> meetjestad:SI7021
- J17: footprint 632723300011_Eagle_WR-USB_rev20b:632723100011 -> meetjestad:USB-C_new
- J3: value Prototype header -> Conn_01x02_Male; footprint Connector_PinSocket_2.54mm:PinSocket_1x15_P2.54mm_Vertical -> Connector_PinHeader_2.54mm:PinHeader_1x02_P2.54mm_Vertical
- J4: footprint Connector_PinSocket_2.54mm:PinSocket_1x04_P2.54mm_Vertical -> meetjestad:OLED_1.3
- J6: footprint Connector_PinHeader_2.54mm:PinHeader_1x02_P2.54mm_Vertical -> meetjestad:Combi_2.0_2.45pitch_2PIN
- Logo_kitt1: moved to F.Cu
- Logo_mjs1: footprint meetjestad:mjs_logo -> meetjestad:mjs-logo-16mm; moved to B.Cu
- R15: value 10k -> 3k3
- R24: value 1M -> 100k
- R25: value 100k -> 10k
- R34, R35, R36: value 1k -> 3k3
- R43, R44, R45: value 10k -> 1k
- R46: value 10k -> 1M
- SP2: footprint Jumper:SolderJumper-2_P1.3mm_Open_TrianglePad1.0x1.5mm -> Jumper:SolderJumper-2_P1.3mm_Bridged_RoundedPad1.0x1.5mm; moved to F.Cu
- U5: value STM32L072RBTx-meetjestad -> STM32L072RZTx-meetjestad
- e1: renamed from SP1; footprint Jumper:SolderJumper-2_P1.3mm_Open_TrianglePad1.0x1.5mm -> Jumper:SolderJumper-2_P1.3mm_Bridged_RoundedPad1.0x1.5mm; moved to F.Cu
- moved H2 126.2 mm to (203.3, 64.5)
- moved H1 125.7 mm to (84.8, 108.7)
- moved Logo_kitt1 123.2 mm to (208.3, 92.1), turned to 90 degrees
- moved R43 78.1 mm to (99.2, 115.7)
- moved Logo_mjs1 63.5 mm to (175.8, 94.2), turned to 270 degrees
- moved J3 57.7 mm to (129.5, 86.4), turned to 90 degrees
- moved R25 57.7 mm to (118.4, 74.9), turned to 0 degrees
- moved J14 56.1 mm to (86.4, 114.3), turned to 90 degrees
- moved R6 52.5 mm to (93.3, 77.1), turned to 90 degrees
- moved J12 43.1 mm to (144.8, 71.1), turned to 90 degrees
- moved R24 41.4 mm to (135.4, 86.2), turned to 0 degrees
- moved J4 35.9 mm to (144.8, 86.4), turned to 270 degrees
- moved J6 33.3 mm to (137.2, 68.6)
- moved R45 30.6 mm to (169.2, 105.7), turned to 0 degrees
- moved R44 28.6 mm to (169.2, 103.6), turned to 0 degrees
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- renumbered PSU3 to PSU1, PSU4 to PSU3, PSU2 to PSU4
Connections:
- J12 pad 2: PA13 -> PA14
- J12 pad 3: NRST -> GND
- J12 pad 4: PA14 -> PA13
- J12 pad 5: GND -> NRST
- J3 pad 1: PB6 -> Vin
- J3 pad 2: PB7 -> Net-(J3-Pad2)
- J8 pad 1: 5V-sw -> VBUS
- PSU1 pad 3: Net-(PSU3-Pad3) -> Net-(J3-Pad2)
- PSU4 pad 1: PC10 -> PC12
- R1 pad 1: Net-(PSU3-Pad3) -> Net-(R1-Pad1)
- R1 pad 2: Vin -> PC13
- R11 pad 1: PC10 -> PC12
- R2 pad 1: PC2 -> PH0
- R24 pad 1: 3V-sw_sens -> Net-(J3-Pad2)
- R24 pad 2: PB0 -> GND
- R25 pad 1: PB0 -> Net-(D5-Pad1)
- R25 pad 2: GND -> Net-(R25-Pad2)
- R43 pad 1: PB15 -> PA0
- R43 pad 2: Net-(R43-Pad2) -> Net-(R2-Pad2)
- R44 pad 1: PB14 -> PA4
- R45 pad 1: PB13 -> PA5
- R46 pad 1: PB12 -> VBUS
- R46 pad 2: Net-(R46-Pad2) -> PA7
- U2 pad 5: PA15 -> PC2
- U2 pad 6: PA7 -> Net-(R1-Pad1)
- U5 pad 2: Net-(U5-Pad2) -> PC13
- U5 pad 53: Net-(U5-Pad53) -> PC12
- U6 pad 1: PC9 -> Net-(R25-Pad2)
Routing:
- net VBUS: track 37.7 -> 141.6 mm, vias 0 -> 2
- net PH0: track 0.00 -> 87.8 mm, vias 0 -> 2
- net PA0: track 28.0 -> 86.3 mm
- net PA13: track 69.2 -> 17.1 mm, vias 2 -> 1
- net PC12: track 0.00 -> 42.9 mm, vias 0 -> 3
- net PC2: track 83.8 -> 44.8 mm
- net PC13: track 0.00 -> 35.7 mm, vias 0 -> 2
- net PC9: track 80.6 -> 45.3 mm, vias 2 -> 0
- net PA14: track 55.9 -> 20.8 mm, vias 0 -> 1
- net PB7: track 98.4 -> 133.3 mm
- net PA15: track 23.3 -> 54.8 mm, vias 0 -> 2
- net PH1: track 0.00 -> 30.6 mm, vias 0 -> 2
- net PA5: track 87.6 -> 59.7 mm, vias 1 -> 2
- net PB6: track 100.0 -> 125.8 mm, vias 3 -> 2
- net PB15: track 55.5 -> 30.5 mm, vias 3 -> 0
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- added copper zone on F.Cu, net Net-(C22-Pad1)
- added copper zone on F.Cu, net Net-(C29-Pad1)
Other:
- board size 125.7 x 56.5 mm -> 141.1 x 56 mm
- net class PA11 added: clearance 0.15, trace_width 0.25, via_dia 0.7, via_drill 0.35
- net class PA12 added: clearance 0.15, trace_width 0.25, via_dia 0.7, via_drill 0.35
- net class USBC added: clearance 0.15, trace_width 0.25, via_dia 0.7, via_drill 0.35
- rule trace_min: 0.2 -> 0.15
- rule via_min_size: 0.4 -> 0.35
- board text added: "!∿A0"
- board text added: "!∿A1"
- board text added: "!⎍SCL1"
- board text added: "!⎍SDA1"
- board text added: "Analog input Digital input/output I²C with 3V pullups I²C1 with ⌥5V pullups I²C2 with ⌥3V pullups PWM output DAC, not 5V tolerant Analog input Always on power Switchable power Digital I/O"
- board text added: "Ax Dx SDA, SCL !SDA1, !SCL1 SDA2, SCL2 ⎍ !∿ TX4 3V ⌥3V, ⌥5V All except power"
- board text added: "Button"
- board text added: "Debug"
- board text added: "MJS 2020 Proto3 Eng. M.F. Rijkeboer"
- board text added: "MOSI1"
- board text added: "NRST"
- board text added: "NSS1"
- board text added: "Pin legend"
- board text added: "Power On/Off ▶"
- board text added: "RESET"
- board text added: "RX1"
- board text added: "Radio"
- board text added: "SCL1"
- board text added: "SCL2"
- board text added: "SCL2 PU"
- board text added: "SDA1"
- board text added: "SDA2"
- board text added: "SDA2 PU"
- board text added: "SPS030"
- board text added: "SWCLK"
- board text added: "SWD"
- board text added: "SWDIO"
- board text added: "SX1262"
- board text added: "TX1"
- board text added: "TX4"
- board text added: "User interaction"
- board text added: "VUSB"
- board text added: "⌥3V"
- board text added: "⌥3V_GPS"
- board text added: "⌥5V"
- board text added: "⎍D0"
- board text added: "⎍MISO1"
- board text added: "⎍RX4"
- board text added: "⎍SCK1"
- board text removed: "3V_perm"
- board text removed: "3V_sw"
- board text removed: "3V_sw_GPS"
- board text removed: "3V_sw_sens"
- board text removed: "5V_sw"
- board text removed: "A0"
- board text removed: "A1"
- board text removed: "A3"
- board text removed: "A4"
- board text removed: "A5"
- board text removed: "A6"
- board text removed: "Connectivity"
- board text removed: "D0"
- board text removed: "D3"
- board text removed: "D4"
- board text removed: "D5"
- board text removed: "D6"
- board text removed: "D7"
- board text removed: "D8"
- board text removed: "D9"
- board text removed: "I2C1"
- board text removed: "I2C2"
- board text removed: "I2C2_SCL"
- board text removed: "I2C2_SDA"
- board text removed: "LoRa1262-868 G-NiceRF"
- board text removed: "MJS 2020 Proto_2 Eng. M.F. Rijkeboer"
- board text removed: "Particulate matter"
- board text removed: "RX"
- board text removed: "SPI1_MISO"
- board text removed: "SPI1_MOSI"
- board text removed: "SPI1_NSS"
- board text removed: "SPI1_SCK"
- board text removed: "TX"

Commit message: Update to MJS2020-PROTO4
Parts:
- removed J17: USB_C_connector, meetjestad:USB-C_new
- added J11: USBC(2.0), meetjestad:DX07S016JA3R1500, F.Cu at (86.3, 67.7)
- H1, H2, H3: footprint MountingHole:MountingHole_3.2mm_M3 -> meetjestad:MountingHole_3.2mm_M3
- J15: footprint meetjestad:SI7021 -> meetjestad2:SI7021
- J16, J3: footprint Connector_PinHeader_2.54mm:PinHeader_1x02_P2.54mm_Vertical -> meetjestad:PinHeader_Male_1X2
- J2: footprint Connector_PinSocket_2.54mm:PinSocket_1x16_P2.54mm_Vertical -> meetjestad:PinHeader_Female_1X16
- J5: footprint meetjestad:Battery__holder -> meetjestad2:Battery__holder
- J8, J9: footprint Connector_PinSocket_2.54mm:PinSocket_1x06_P2.54mm_Vertical -> meetjestad:PinHeader_Female_1X6
- SW1, SW2: footprint Button_Switch_THT:SW_PUSH_6mm -> meetjestad:SW_Push_6mm
- moved FID3 10.3 mm to (203.6, 78.0)
- moved D4 7.80 mm to (112.5, 71.2), turned to 270 degrees
- moved C27 0.78 mm to (112.3, 70.7)
- moved Logo_mjs2 0.72 mm to (145.7, 103.8), turned to 0 degrees
- moved Logo_kitt1 0.63 mm to (207.6, 92.1)
- moved C30 0.54 mm to (116.2, 66.5)
- moved FID1 0.28 mm to (81.2, 117.0)
- moved C31 0.13 mm to (140.3, 72.4)
- renumbered e1 to SP1
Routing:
- net GND: track 207.1 -> 268.8 mm, vias 90 -> 107
- net Net-(C27-Pad2): track 18.8 -> 7.82 mm
- net Net-(J11-Pad6): track 16.7 -> 12.6 mm, vias 1 -> 0
- net Net-(J11-Pad3): track 5.42 -> 9.02 mm
- net VBUS: track 141.6 -> 144.8 mm, vias 2 -> 4
- net Net-(J11-Pad5): track 16.3 -> 14.5 mm, vias 2 -> 0
- net Net-(J11-Pad9): track 10.00 -> 8.64 mm
- net 3V-perm_CPU: track 94.8 -> 95.9 mm
- net PA10: track 16.7 -> 17.2 mm
- added copper zone on B.Cu, net GND
- added copper zone on F.Cu, net Net-(C27-Pad2)
- added copper zone on F.Cu, net PB6
- added copper zone on F.Cu, net PB7
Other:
- board text added: "Charge LED ▶"
- board text added: "Charger"
- board text added: "MJS 2020 Proto4 Eng. M.F. Rijkeboer"
- board text added: "TX3"
- board text added: "⎍RX3"
- board text removed: "MJS 2020 Proto3 Eng. M.F. Rijkeboer"
- board text removed: "TX4"
- board text removed: "⎍RX4"
